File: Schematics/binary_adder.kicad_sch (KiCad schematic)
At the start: 32 parts, among them SW1 SW_Push, SW2 SW_Push, U1 4040, U2 LM555xN

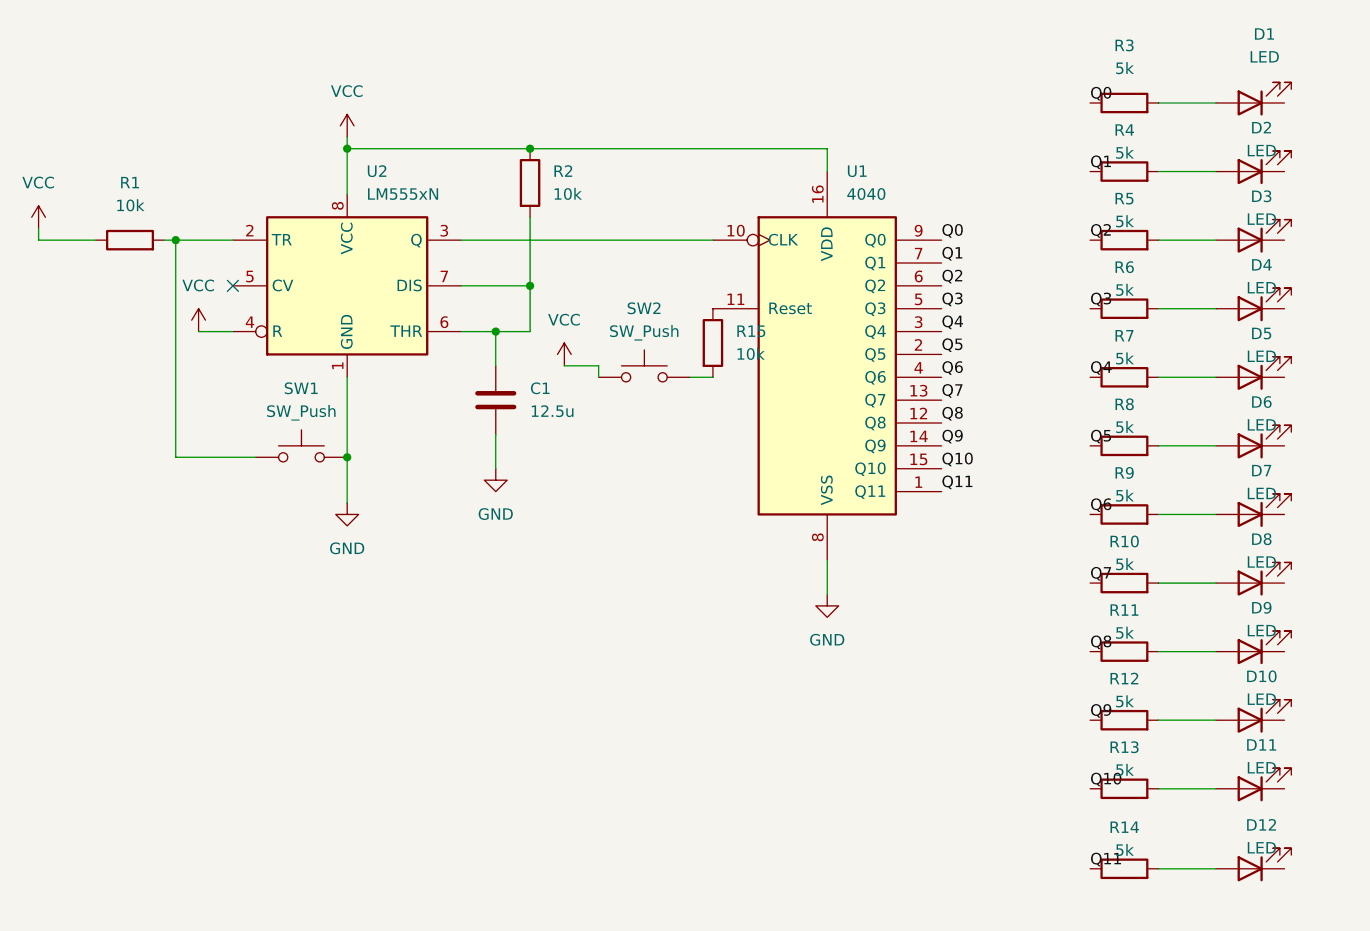
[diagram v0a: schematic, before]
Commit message: Fix GND pull resistor in schematic
Also add ground pour
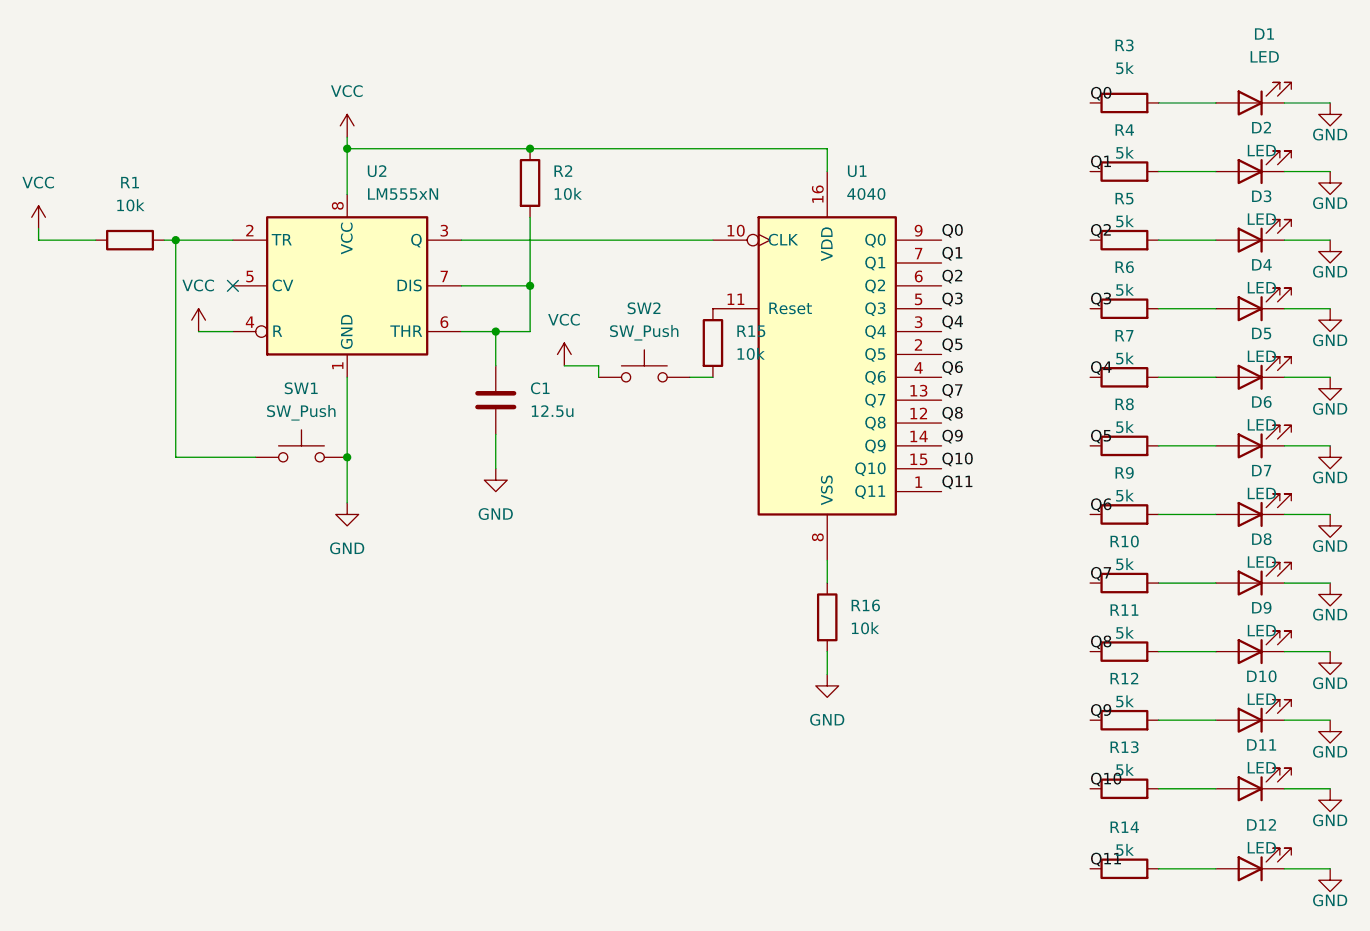
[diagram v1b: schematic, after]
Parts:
- added R16: 10k, Resistor_THT:R_Axial_DIN0204_L3.6mm_D1.6mm_P7.62mm_Horizontal, symbol Device:R
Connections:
- net GND: now also D1.1 (K), D10.1 (K), D11.1 (K), D12.1 (K), D2.1 (K), D3.1 (K), D4.1 (K), D5.1 (K), D6.1 (K), D7.1 (K), D8.1 (K), D9.1 (K), R16.2; no longer U1.8 (VSS)
- new net: R16.1, U1.8 (VSS)

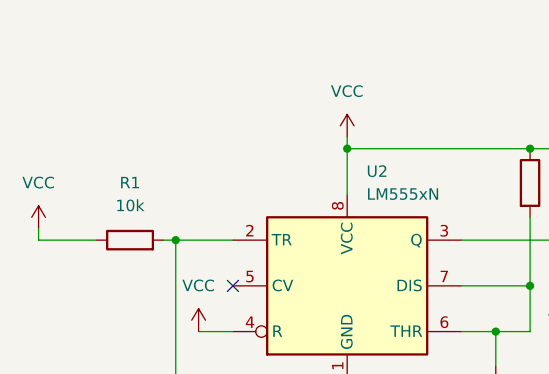
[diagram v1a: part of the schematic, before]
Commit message: Add missing power connector
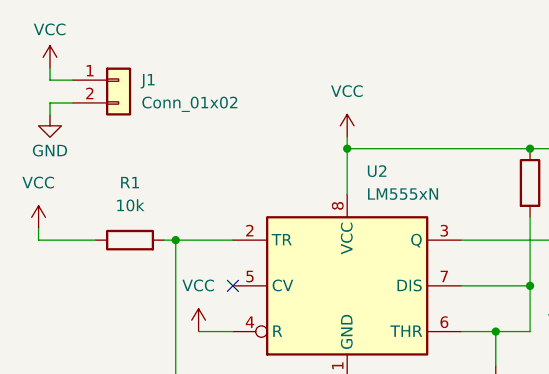
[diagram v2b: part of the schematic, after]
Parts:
- added J1: Conn_01x02, Connector_PinHeader_2.54mm:PinHeader_1x02_P2.54mm_Vertical, symbol Connector_Generic:Conn_01x02
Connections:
- net GND: now also J1.2 (Pin_2)
- net VCC: now also J1.1 (Pin_1)
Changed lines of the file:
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@@
 	(wire
 		(pts
+			(xy 22.86 21.59) (xy 25.4 21.59)
+		)
+		(stroke
+			(width 0)
+			(type default)
+		)
+	)
+	(wire
+		(pts
 			(xy 109.22 82.55) (xy 109.22 85.09)
 		)
@@
 	(wire
 		(pts
+			(xy 22.86 19.05) (xy 25.4 19.05)
+		)
+		(stroke
+			(width 0)
+			(type default)
+		)
+	)
+	(wire
+		(pts
 			(xy 160.02 97.79) (xy 165.1 97.79)
 		)
@@
 	(wire
 		(pts
+			(xy 22.86 17.78) (xy 22.86 19.05)
+		)
+		(stroke
+			(width 0)
+			(type default)
+		)
+	)
+	(wire
+		(pts
 			(xy 160.02 52.07) (xy 165.1 52.07)
 		)
@@
 	(wire
 		(pts
+			(xy 22.86 22.86) (xy 22.86 21.59)
+		)
+		(stroke
+			(width 0)
+			(type default)
+		)
+	)
+	(wire
+		(pts
 			(xy 76.2 41.91) (xy 76.2 46.99)
 		)
@@
 	)
 	(symbol
+		(lib_id "power:GND")
+		(at 22.86 22.86 0)
+		(unit 1)
+		(exclude_from_sim no)
+		(in_bom yes)
+		(on_board yes)
+		(dnp no)
+		(property "Reference" "#PWR021"
+			(at 22.86 29.21 0)
+			(effects
+				(font
+					(size 1.27 1.27)
+				)
+				(hide yes)
+			)
+		)
+		(property "Value" "GND"
+			(at 22.86 26.924 0)
+			(effects
+				(font
+					(size 1.27 1.27)
+				)
+			)
+		)
+		(property "Footprint" ""
+			(at 22.86 22.86 0)
+			(effects
+				(font
+					(size 1.27 1.27)
+				)
+				(hide yes)
+			)
+		)
+		(property "Datasheet" ""
+			(at 22.86 22.86 0)
+			(effects
+				(font
+					(size 1.27 1.27)
+				)
+				(hide yes)
+			)
+		)
+		(property "Description" "Power symbol creates a global label with name \"GND\" , ground"
+			(at 22.86 22.86 0)
+			(effects
+				(font
+					(size 1.27 1.27)
+				)
+				(hide yes)
+			)
+		)
+		(pin "1"
+		)
+		(instances
+			(project ""
+				(path "/b3a9ba6c-8330-4a6b-a1ac-bc265156909f"
+					(reference "#PWR021")
+					(unit 1)
+				)
+			)
+		)
+	)
+	(symbol
 		(lib_id "Device:LED")
 		(at 156.21 44.45 180)
@@
 	)
 	(symbol
+		(lib_id "Connector_Generic:Conn_01x02")
+		(at 30.48 19.05 0)
+		(unit 1)
+		(exclude_from_sim no)
+		(in_bom yes)
+		(on_board yes)
+		(dnp no)
+		(fields_autoplaced yes)
+		(property "Reference" "J1"
+			(at 33.02 19.0499 0)
+			(effects
+				(font
+					(size 1.27 1.27)
+				)
+				(justify left)
+			)
+		)
+		(property "Value" "Conn_01x02"
+			(at 33.02 21.5899 0)
+			(effects
+				(font
+					(size 1.27 1.27)
+				)
+				(justify left)
+			)
+		)
+		(property "Footprint" "Connector_PinHeader_2.54mm:PinHeader_1x02_P2.54mm_Vertical"
+			(at 30.48 19.05 0)
+			(effects
+				(font
+					(size 1.27 1.27)
+				)
+				(hide yes)
+			)
+		)
+		(property "Datasheet" "~"
+			(at 30.48 19.05 0)
+			(effects
+				(font
+					(size 1.27 1.27)
+				)
+				(hide yes)
+			)
+		)
+		(property "Description" "Generic connector, single row, 01x02, script generated (kicad-library-utils/schlib/autogen/connector/)"
+			(at 30.48 19.05 0)
+			(effects
+				(font
+					(size 1.27 1.27)
+				)
+				(hide yes)
+			)
+		)
+		(pin "2"
+		)
+		(pin "1"
+		)
+		(instances
+			(project ""
+				(path "/b3a9ba6c-8330-4a6b-a1ac-bc265156909f"
+					(reference "J1")
+					(unit 1)
+				)
+			)
+		)
+	)
+	(symbol
 		(lib_id "Device:R")
 		(at 31.75 36.83 90)
@@
 					(unit 1)
 				)
+			)
+		)
+	)
+	(symbol
+		(lib_id "power:VCC")
+		(at 22.86 17.78 0)
+		(unit 1)
+		(exclude_from_sim no)
+		(in_bom yes)
+		(on_board yes)
+		(dnp no)
+		(property "Reference" "#PWR020"
+			(at 22.86 21.59 0)
+			(effects
+				(font
+					(size 1.27 1.27)
+				)
+				(hide yes)
+			)
+		)
+		(property "Value" "VCC"
+			(at 22.86 13.462 0)
+			(effects
+				(font
+					(size 1.27 1.27)
+				)
+			)
+		)
+		(property "Footprint" ""
+			(at 22.86 17.78 0)
+			(effects
+				(font
+					(size 1.27 1.27)
+				)
+				(hide yes)
+			)
+		)
+		(property "Datasheet" ""
+			(at 22.86 17.78 0)
+			(effects
+				(font
+					(size 1.27 1.27)
+				)
+				(hide yes)
+			)
+		)
+		(property "Description" "Power symbol creates a global label with name \"VCC\""
+			(at 22.86 17.78 0)
+			(effects
+				(font
+					(size 1.27 1.27)
+				)
+				(hide yes)
+			)
+		)
+		(pin "1"
+		)
+		(instances
+			(project ""
+				(path "/b3a9ba6c-8330-4a6b-a1ac-bc265156909f"
+					(reference "#PWR020")
+					(unit 1)
+				)
